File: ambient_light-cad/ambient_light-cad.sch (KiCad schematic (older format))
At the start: 1 part

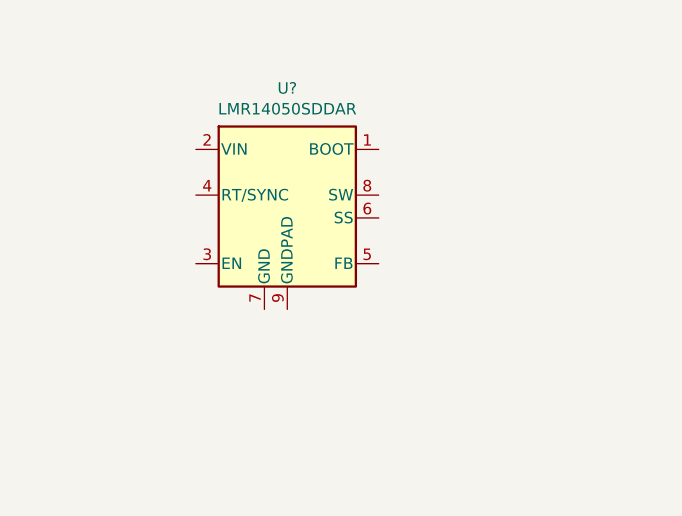
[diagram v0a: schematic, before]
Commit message: Add dc jack
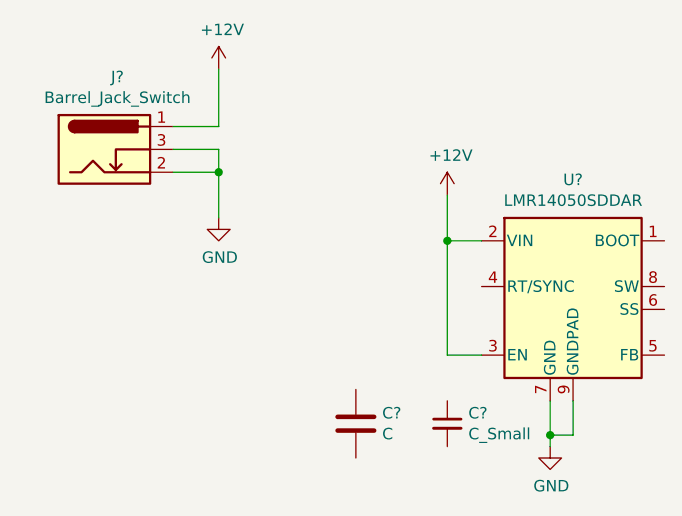
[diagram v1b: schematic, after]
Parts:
- added C?: C_Small, symbol Device:C_Small
- added C?: C, symbol Device:C
- added J?: Barrel_Jack_Switch, symbol Connector:Barrel_Jack_Switch
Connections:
- net +12V: now reaches U?.2 (VIN)
- net +12V: now also U?.3 (EN), J?.1
- net GND: now reaches U?.7 (GND)
- net GND: now also U?.9 (GNDPAD), J?.2, J?.3
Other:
- moved on the sheet: U?
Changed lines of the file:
@@
 L Regulator_Switching:LMR14050SDDAR U?
 U 1 1 5F8C0E9F
-P 2000 1700
-F 0 "U?" H 2000 2167 50  0000 C CNN
-F 1 "LMR14050SDDAR" H 2000 2076 50  0000 C CNN
-F 2 "Package_SO:TI_SO-PowerPAD-8_ThermalVias" H 2050 1250 50  0001 L CIN
-F 3 "http://www.ti.com/lit/ds/symlink/tps54360.pdf" H 2000 1700 50  0001 C CNN
-	1    2000 1700
+P 3250 2100
+F 0 "U?" H 3250 2567 50  0000 C CNN
+F 1 "LMR14050SDDAR" H 3250 2476 50  0000 C CNN
+F 2 "Package_SO:TI_SO-PowerPAD-8_ThermalVias" H 3300 1650 50  0001 L CIN
+F 3 "http://www.ti.com/lit/ds/symlink/tps54360.pdf" H 3250 2100 50  0001 C CNN
+	1    3250 2100
 	1    0    0    -1
 $EndComp
+$Comp
+L power:GND #PWR0101
+U 1 1 5F8C56C2
+P 3150 2800
+F 0 "#PWR0101" H 3150 2550 50  0001 C CNN
+F 1 "GND" H 3155 2627 50  0000 C CNN
+F 2 "" H 3150 2800 50  0001 C CNN
+F 3 "" H 3150 2800 50  0001 C CNN
+	1    3150 2800
+	1    0    0    -1
+$EndComp
+Wire Wire Line
+	3150 2600 3150 2750
+Wire Wire Line
+	3250 2600 3250 2750
+Wire Wire Line
+	3250 2750 3150 2750
+Connection ~ 3150 2750
+Wire Wire Line
+	3150 2750 3150 2800
+$Comp
+L Connector:Barrel_Jack_Switch J?
+U 1 1 5F8C7BF5
+P 1200 1500
+F 0 "J?" H 1257 1817 50  0000 C CNN
+F 1 "Barrel_Jack_Switch" H 1257 1726 50  0000 C CNN
+F 2 "" H 1250 1460 50  0001 C CNN
+F 3 "~" H 1250 1460 50  0001 C CNN
+	1    1200 1500
+	1    0    0    -1
+$EndComp
+$Comp
+L power:+12V #PWR?
+U 1 1 5F8CB187
+P 1700 1150
+F 0 "#PWR?" H 1700 1000 50  0001 C CNN
+F 1 "+12V" H 1715 1323 50  0000 C CNN
+F 2 "" H 1700 1150 50  0001 C CNN
+F 3 "" H 1700 1150 50  0001 C CNN
+	1    1700 1150
+	1    0    0    -1
+$EndComp
+Wire Wire Line
+	1700 1150 1700 1400
+Wire Wire Line
+	1700 1400 1500 1400
+$Comp
+L power:GND #PWR?
+U 1 1 5F8CCC7D
+P 1700 1800
+F 0 "#PWR?" H 1700 1550 50  0001 C CNN
+F 1 "GND" H 1705 1627 50  0000 C CNN
+F 2 "" H 1700 1800 50  0001 C CNN
+F 3 "" H 1700 1800 50  0001 C CNN
+	1    1700 1800
+	1    0    0    -1
+$EndComp
+Wire Wire Line
+	1700 1800 1700 1600
+Wire Wire Line
+	1700 1600 1500 1600
+Wire Wire Line
+	1500 1500 1700 1500
+Wire Wire Line
+	1700 1500 1700 1600
+Connection ~ 1700 1600
+$Comp
+L power:+12V #PWR?
+U 1 1 5F8D58E9
+P 2700 1700
+F 0 "#PWR?" H 2700 1550 50  0001 C CNN
+F 1 "+12V" H 2715 1873 50  0000 C CNN
+F 2 "" H 2700 1700 50  0001 C CNN
+F 3 "" H 2700 1700 50  0001 C CNN
+	1    2700 1700
+	1    0    0    -1
+$EndComp
+Wire Wire Line
+	2700 1700 2700 1900
+Wire Wire Line
+	2700 1900 2850 1900
+Wire Wire Line
+	2700 1900 2700 2400
+Wire Wire Line
+	2700 2400 2850 2400
+Connection ~ 2700 1900
+$Comp
+L Device:C_Small C?
+U 1 1 5F8D7B1F
+P 2700 2700
+F 0 "C?" H 2792 2746 50  0000 L CNN
+F 1 "C_Small" H 2792 2655 50  0000 L CNN
+F 2 "" H 2700 2700 50  0001 C CNN
+F 3 "~" H 2700 2700 50  0001 C CNN
+	1    2700 2700
+	1    0    0    -1
+$EndComp
+$Comp
+L Device:C C?
+U 1 1 5F8D965F
+P 2300 2700
+F 0 "C?" H 2415 2746 50  0000 L CNN
+F 1 "C" H 2415 2655 50  0000 L CNN
+F 2 "" H 2338 2550 50  0001 C CNN
+F 3 "~" H 2300 2700 50  0001 C CNN
+	1    2300 2700
+	1    0    0    -1
+$EndComp

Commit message: Changed roll back parts
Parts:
- added C?: Device_C, symbol ambient_light-cad-cache:Device_C
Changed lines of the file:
@@
+	1    0    0    -1
+$EndComp
+$Comp
+L ambient_light-cad-cache:Device_C C?
+U 1 1 5F8EE363
+P 1600 2700
+F 0 "C?" H 1715 2746 50  0000 L CNN
+F 1 "Device_C" H 1715 2655 50  0000 L CNN
+F 2 "" H 1638 2550 50  0001 C CNN
+F 3 "" H 1600 2700 50  0001 C CNN
+	1    1600 2700
 	1    0    0    -1
 $EndComp

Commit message: Change lib
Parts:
- removed C?: Device_C, symbol ambient_light-cad-cache:Device_C
- removed U?: LMR14050SDDAR, Package_SO:TI_SO-PowerPAD-8_ThermalVias, symbol Regulator_Switching:LMR14050SDDAR
- added U?: LMR14050SDDAR, Package_SO:TI_SO-PowerPAD-8_ThermalVias, symbol ambient_light-cad:LMR14050SDDAR
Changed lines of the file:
@@
 $EndDescr
-$Comp
-L Regulator_Switching:LMR14050SDDAR U?
-U 1 1 5F8C0E9F
-P 3250 2100
-F 0 "U?" H 3250 2567 50  0000 C CNN
-F 1 "LMR14050SDDAR" H 3250 2476 50  0000 C CNN
-F 2 "Package_SO:TI_SO-PowerPAD-8_ThermalVias" H 3300 1650 50  0001 L CIN
-F 3 "http://www.ti.com/lit/ds/symlink/tps54360.pdf" H 3250 2100 50  0001 C CNN
-	1    3250 2100
-	1    0    0    -1
-$EndComp
 $Comp
 L power:GND #PWR0101
@@
 $EndComp
 $Comp
-L ambient_light-cad-cache:Device_C C?
-U 1 1 5F8EE363
-P 1600 2700
-F 0 "C?" H 1715 2746 50  0000 L CNN
-F 1 "Device_C" H 1715 2655 50  0000 L CNN
-F 2 "" H 1638 2550 50  0001 C CNN
-F 3 "" H 1600 2700 50  0001 C CNN
-	1    1600 2700
+L ambient_light-cad:LMR14050SDDAR U?
+U 1 1 5F91AED1
+P 3250 2100
+F 0 "U?" H 3250 2567 50  0000 C CNN
+F 1 "LMR14050SDDAR" H 3250 2476 50  0000 C CNN
+F 2 "Package_SO:TI_SO-PowerPAD-8_ThermalVias" H 3300 1650 50  0001 L CIN
+F 3 "http://www.ti.com/lit/ds/symlink/tps54360.pdf" H 3250 2100 50  0001 C CNN
+	1    3250 2100
 	1    0    0    -1
 $EndComp

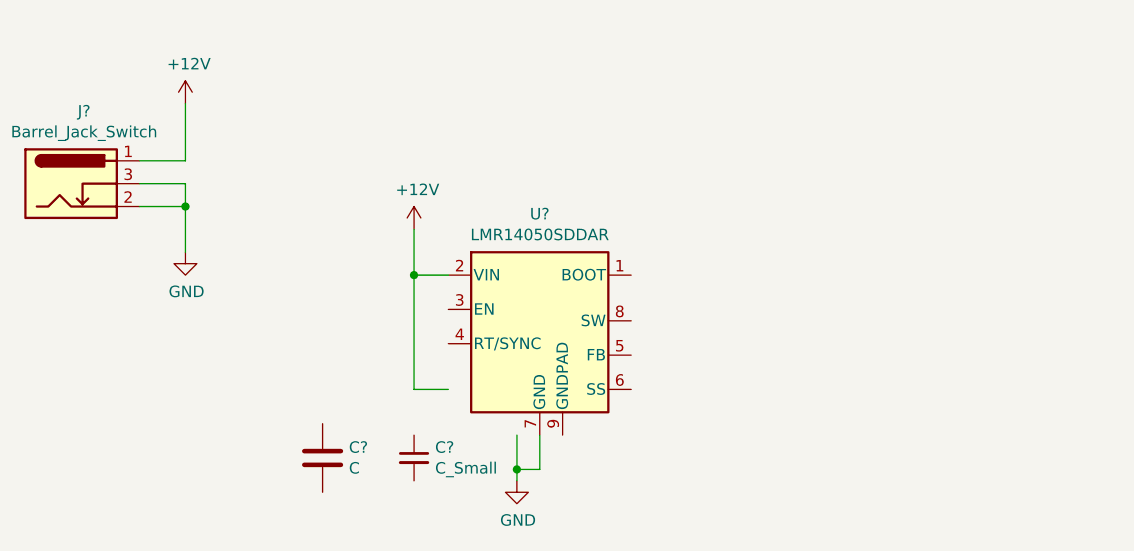
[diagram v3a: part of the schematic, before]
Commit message: Add Power management example
기본적인 부품 배치만 완료
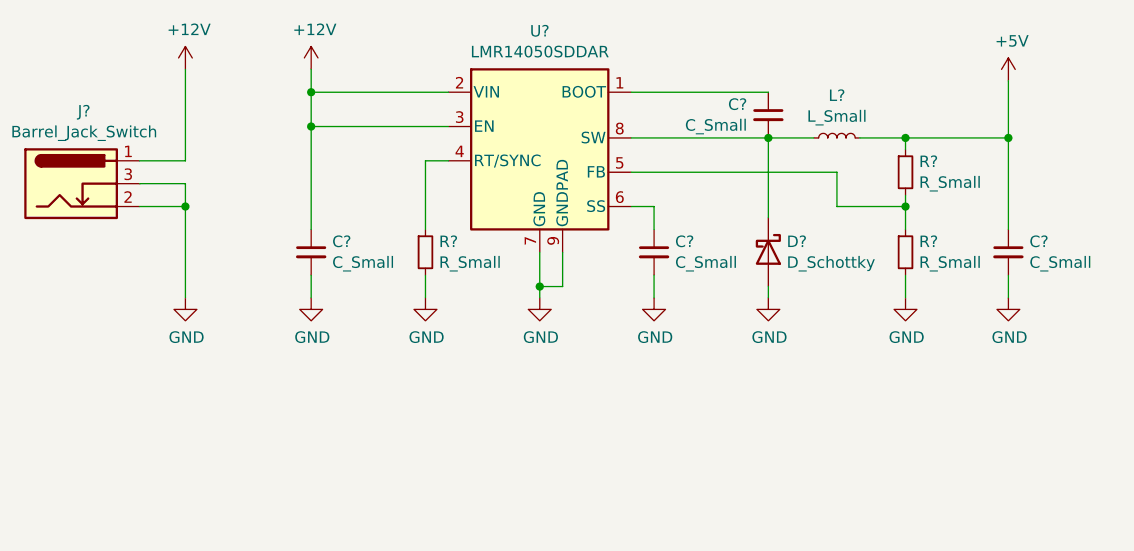
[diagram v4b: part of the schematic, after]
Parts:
- removed C?: C, symbol Device:C
- removed U?: LMR14050SDDAR, Package_SO:TI_SO-PowerPAD-8_ThermalVias, symbol ambient_light-cad:LMR14050SDDAR
- added C? (x3): C_Small, symbol Device:C_Small
- added D?: D_Schottky, symbol Device:D_Schottky
- added L?: L_Small, symbol Device:L_Small
- added R? (x3): R_Small, symbol Device:R_Small
- added U?: LMR14050SDDAR, Package_SO:TI_SO-PowerPAD-8_ThermalVias, symbol ambient_light-cad:LMR14050SDDAR
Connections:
- net labels added: +5V
- wire segments 14 -> 39
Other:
- moved on the sheet: C?

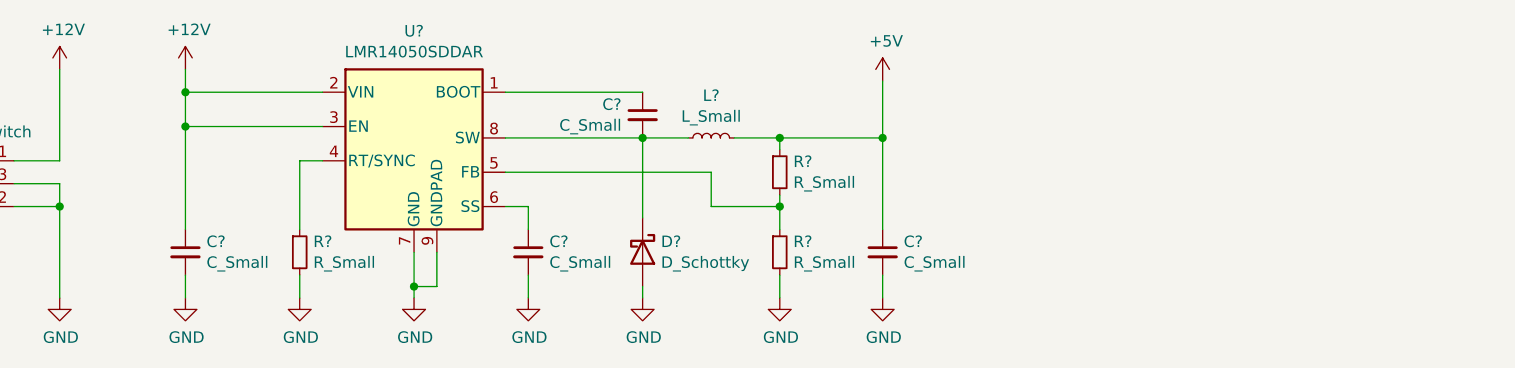
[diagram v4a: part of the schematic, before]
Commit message: [Added] LMR14050 component
저항, 커패시터, 인덕터 선정
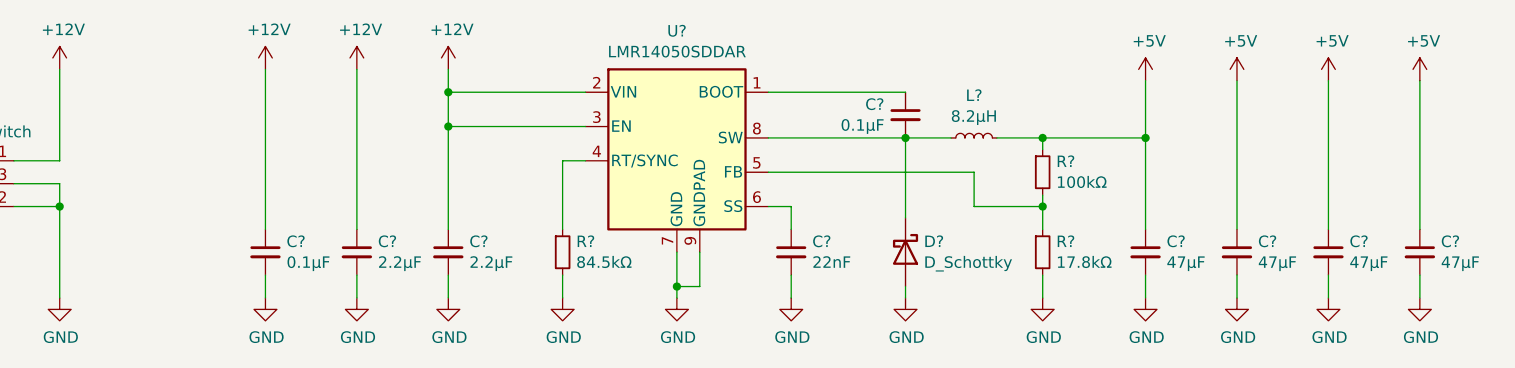
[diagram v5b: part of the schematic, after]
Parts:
- added C? (x3): 47μF, symbol Device:C_Small
- added C?: 2.2μF, symbol Device:C_Small
- added C?: 0.1μF, symbol Device:C_Small
- C?: value C_Small -> 22nF
- C?: value C_Small -> 47μF
- C?: value C_Small -> 0.1μF
- C?: value C_Small -> 2.2μF
- L?: value L_Small -> 8.2μH
- R?: value R_Small -> 84.5kΩ
- R?: value R_Small -> 17.8kΩ
- R?: value R_Small -> 100kΩ
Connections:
- net +12V: now also C?.1, C?.1
- net +5V: now also C?.1, C?.1, C?.1
- net GND: now also C?.2, C?.2, C?.2, C?.2, C?.2
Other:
- moved on the sheet: C?, D?, L?, R?, U?

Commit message: [Updated] Select shottky diode
SS54CF - DO - 214AB(SMC)
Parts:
- D?: value D_Schottky -> SS54CF
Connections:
- net +12V: no longer U?.3 (EN)
- no-connect marks 0 -> 1
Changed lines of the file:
@@
 	1    0    0    -1
 $EndComp
-Wire Wire Line
-	3400 1100 3400 1250
 $Comp
 L Device:C_Small C?
@@
 P 5400 1800
 F 0 "D?" V 5354 1880 50  0000 L CNN
-F 1 "D_Schottky" V 5445 1880 50  0000 L CNN
+F 1 "SS54CF" V 5445 1880 50  0000 L CNN
 F 2 "" H 5400 1800 50  0001 C CNN
 F 3 "~" H 5400 1800 50  0001 C CNN
@@
 	0    1    1    0
 $EndComp
-Connection ~ 3400 1250
-Wire Wire Line
-	3400 1250 3400 1700
 Wire Wire Line
 	3900 1400 3900 1700
@@
 Wire Wire Line
 	3400 1100 4000 1100
-Wire Wire Line
-	3400 1250 4000 1250
 Wire Wire Line
 	4900 2000 4900 1900
@@
 Wire Wire Line
 	2600 1000 2600 1700
+Wire Wire Line
+	3400 1100 3400 1700
+NoConn ~ 4000 1250
 $EndSCHEMATC

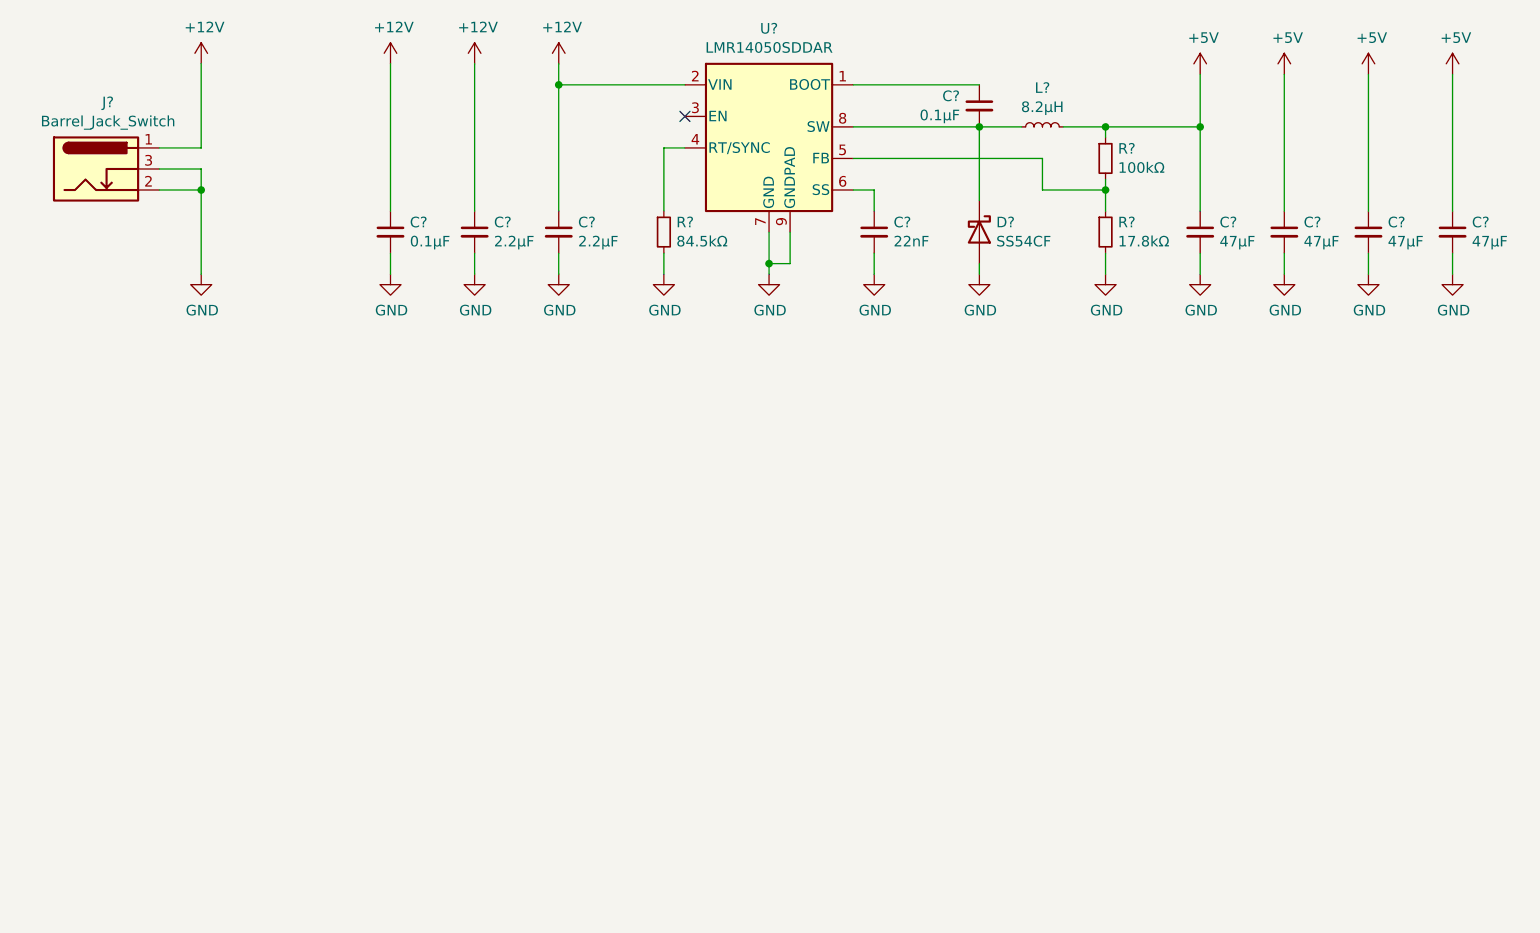
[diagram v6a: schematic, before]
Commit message: [Added] Power file separation
make size A4
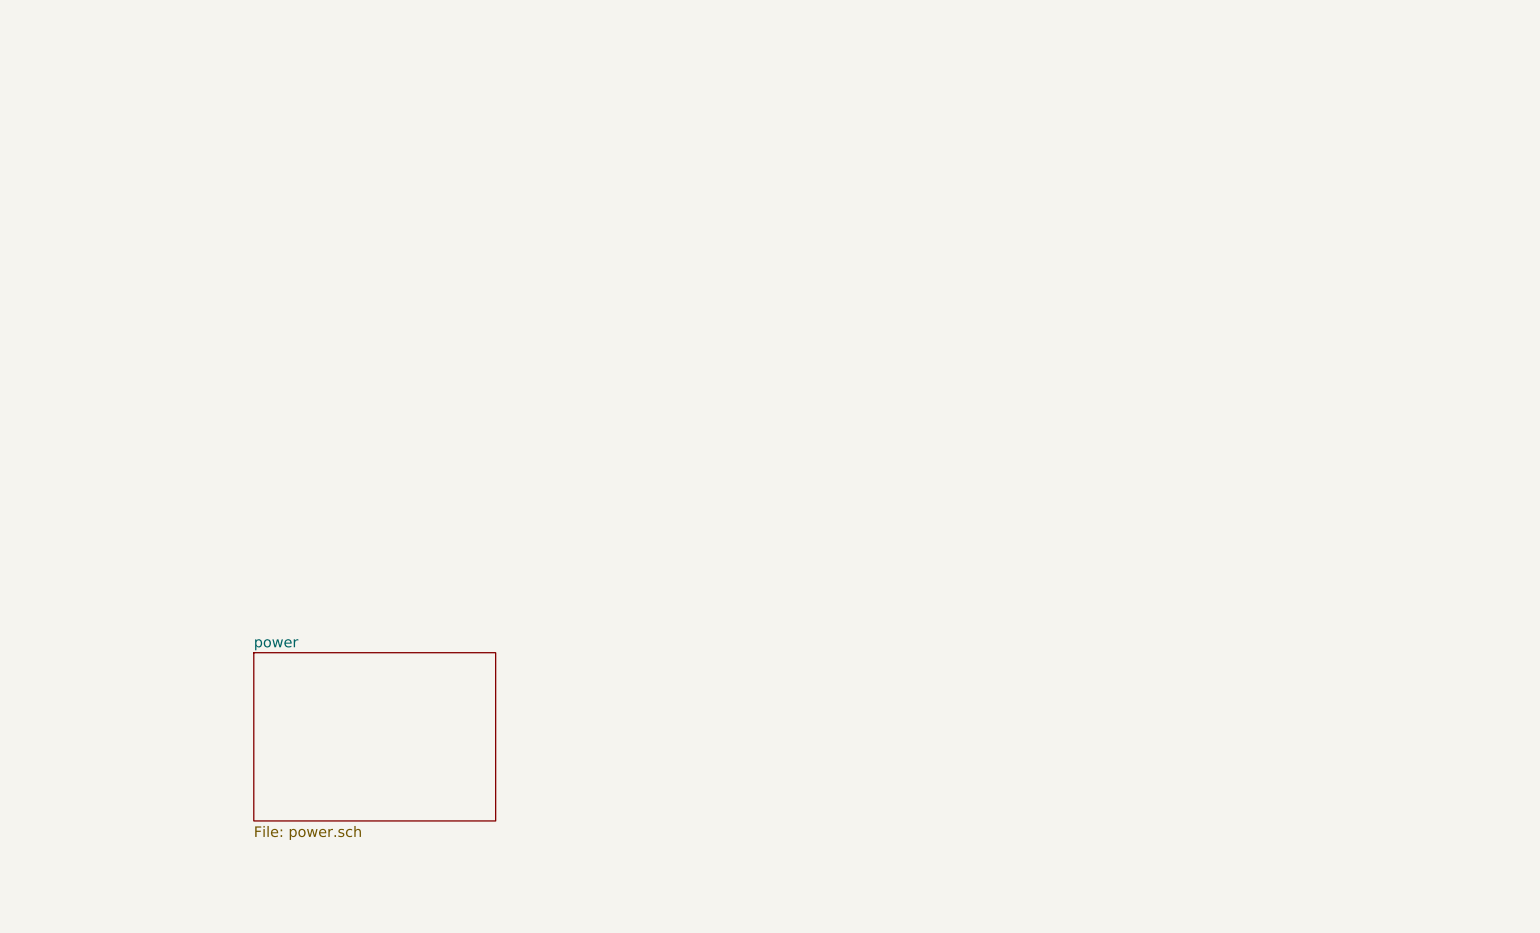
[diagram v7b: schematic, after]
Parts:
- removed C?: 22nF, symbol Device:C_Small
- removed C? (x4): 47μF, symbol Device:C_Small
- removed C? (x2): 0.1μF, symbol Device:C_Small
- removed C? (x2): 2.2μF, symbol Device:C_Small
- removed D?: SS54CF, symbol Device:D_Schottky
- removed J?: Barrel_Jack_Switch, symbol Connector:Barrel_Jack_Switch
- removed L?: 8.2μH, symbol Device:L_Small
- removed R?: 84.5kΩ, symbol Device:R_Small
- removed R?: 17.8kΩ, symbol Device:R_Small
- removed R?: 100kΩ, symbol Device:R_Small
- removed U?: LMR14050SDDAR, Package_SO:TI_SO-PowerPAD-8_ThermalVias, symbol ambient_light-cad:LMR14050SDDAR
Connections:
- no-connect marks 1 -> 0

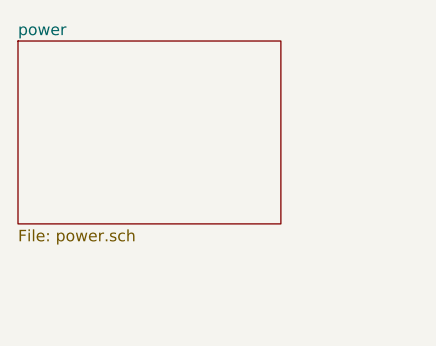
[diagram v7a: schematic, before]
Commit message: [Modified] Align and add Test Point
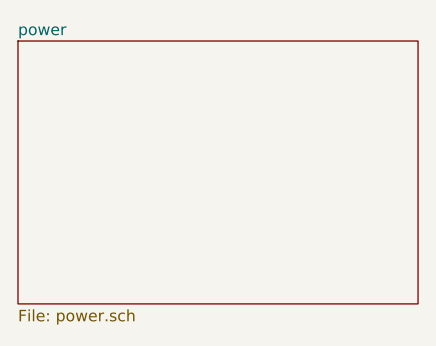
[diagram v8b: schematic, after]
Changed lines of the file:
@@
 $EndDescr
 $Sheet
-S 1950 3800 1150 800
+S 1950 3800 1750 1150
 U 5FDBFA91
 F0 "power" 50
